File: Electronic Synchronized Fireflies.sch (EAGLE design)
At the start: 30 parts, among them J1 2WIRE_HEADER, J2 3WIRE_HEADER, Q1 BSS123, Q2 BSS84, Q3 LPT80A, Q4 LPT80A, Q5 LPT80A, U1 NCP1400A, U2 MSP430G2231

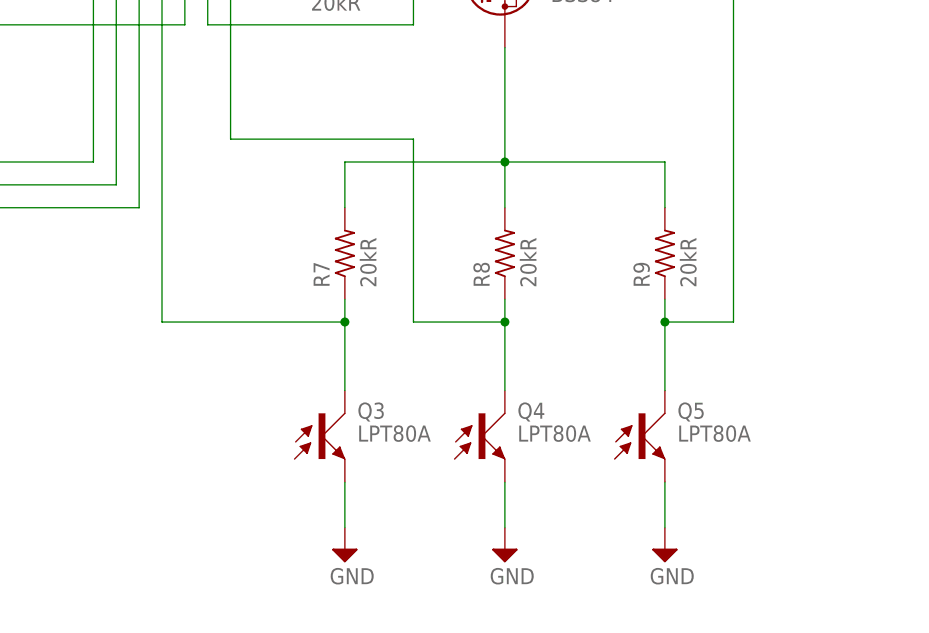
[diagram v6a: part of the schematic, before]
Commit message: Move back to LDR setup
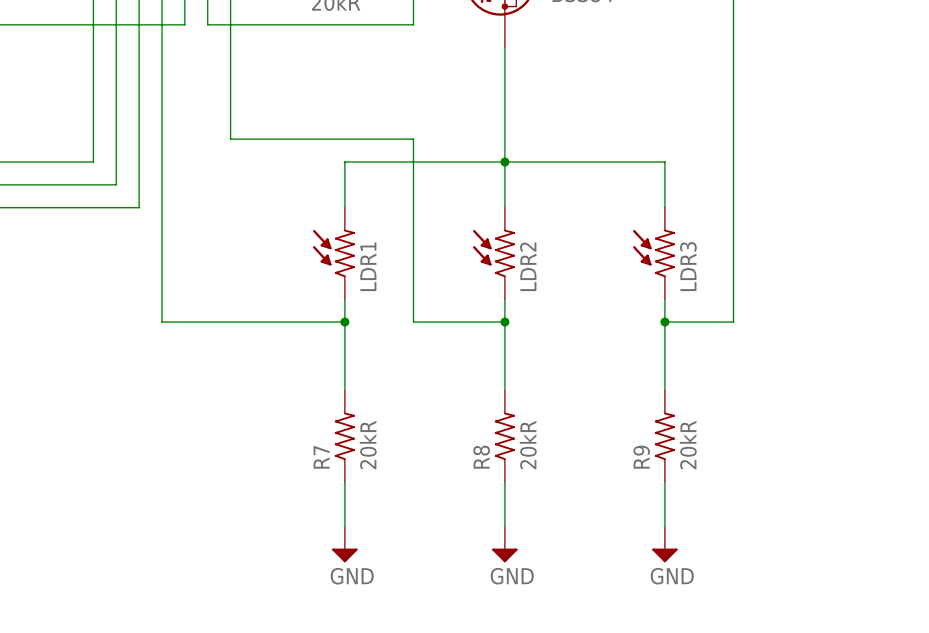
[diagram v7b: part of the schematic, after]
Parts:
- removed Q3, Q4, Q5: LPT80A, Electronic Synchronized Fireflies:LPT80ARTANGLEHOLDER
- added LDR1, LDR2, LDR3: LDRRTANGLEHOLDER, Electronic Synchronized Fireflies:LDRRTANGLEHOLDER
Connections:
- removed net N$14: Q3.C, R7.P$1, U2.6
- new net N$8: LDR1.1, R7.P$2, U2.6
- net GND: now also R7.P$1, R8.P$1, R9.P$1; no longer Q3.E, Q4.E, Q5.E
- net N$12: now also LDR1.2, LDR2.2, LDR3.2; no longer R7.P$2, R8.P$2, R9.P$2
- net N$13: now also LDR2.1, R8.P$2; no longer Q4.C, R8.P$1
- net N$15: now also LDR3.1, R9.P$2; no longer Q5.C, R9.P$1
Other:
- moved on the sheet: R7, R8, R9
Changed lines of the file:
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@@
 <part name="D5" library="Electronic Synchronized Fireflies" deviceset="LED" device="RTANGLEHOLDER" value="LED"/>
 <part name="D6" library="Electronic Synchronized Fireflies" deviceset="LED" device="RTANGLEHOLDER" value="LED"/>
-<part name="Q3" library="Electronic Synchronized Fireflies" deviceset="LPT80A" device="RTANGLEHOLDER" value="LPT80A"/>
-<part name="Q4" library="Electronic Synchronized Fireflies" deviceset="LPT80A" device="RTANGLEHOLDER" value="LPT80A"/>
-<part name="Q5" library="Electronic Synchronized Fireflies" deviceset="LPT80A" device="RTANGLEHOLDER" value="LPT80A"/>
+<part name="LDR1" library="Electronic Synchronized Fireflies" deviceset="LDR" device="RTANGLEHOLDER"/>
+<part name="LDR2" library="Electronic Synchronized Fireflies" deviceset="LDR" device="RTANGLEHOLDER"/>
+<part name="LDR3" library="Electronic Synchronized Fireflies" deviceset="LDR" device="RTANGLEHOLDER"/>
 </parts>
 <sheets>
@@
 <instance part="R5" gate="G$1" x="116.84" y="78.74" rot="R90"/>
 <instance part="R6" gate="G$1" x="129.54" y="78.74" rot="R90"/>
-<instance part="R7" gate="G$1" x="185.42" y="83.82" rot="R90"/>
-<instance part="R8" gate="G$1" x="203.2" y="83.82" rot="R90"/>
-<instance part="R9" gate="G$1" x="220.98" y="83.82" rot="R90"/>
+<instance part="R7" gate="G$1" x="185.42" y="63.5" rot="R90"/>
+<instance part="R8" gate="G$1" x="203.2" y="63.5" rot="R90"/>
+<instance part="R9" gate="G$1" x="220.98" y="63.5" rot="R90"/>
 <instance part="SUPPLY8" gate="GND" x="104.14" y="50.8"/>
 <instance part="SUPPLY9" gate="GND" x="116.84" y="50.8"/>
@@
 <instance part="D5" gate="G$1" x="116.84" y="60.96"/>
 <instance part="D6" gate="G$1" x="129.54" y="60.96"/>
-<instance part="Q3" gate="1" x="182.88" y="63.5"/>
-<instance part="Q4" gate="1" x="200.66" y="63.5"/>
-<instance part="Q5" gate="1" x="218.44" y="63.5"/>
+<instance part="LDR1" gate="G$1" x="185.42" y="83.82" rot="R90"/>
+<instance part="LDR2" gate="G$1" x="203.2" y="83.82" rot="R90"/>
+<instance part="LDR3" gate="G$1" x="220.98" y="83.82" rot="R90"/>
 </instances>
 <busses>
@@
 <pinref part="SUPPLY11" gate="GND" pin="GND"/>
 <wire x1="185.42" y1="58.42" x2="185.42" y2="53.34" width="0.1524" layer="91"/>
-<pinref part="Q3" gate="1" pin="E"/>
+<pinref part="R7" gate="G$1" pin="P$1"/>
 </segment>
 <segment>
 <pinref part="SUPPLY12" gate="GND" pin="GND"/>
 <wire x1="203.2" y1="58.42" x2="203.2" y2="53.34" width="0.1524" layer="91"/>
-<pinref part="Q4" gate="1" pin="E"/>
+<pinref part="R8" gate="G$1" pin="P$1"/>
 </segment>
 <segment>
 <pinref part="SUPPLY13" gate="GND" pin="GND"/>
 <wire x1="220.98" y1="53.34" x2="220.98" y2="58.42" width="0.1524" layer="91"/>
-<pinref part="Q5" gate="1" pin="E"/>
+<pinref part="R9" gate="G$1" pin="P$1"/>
 </segment>
 <segment>
@@
 <wire x1="203.2" y1="106.68" x2="203.2" y2="93.98" width="0.1524" layer="91"/>
 <wire x1="203.2" y1="93.98" x2="185.42" y2="93.98" width="0.1524" layer="91"/>
-<pinref part="R7" gate="G$1" pin="P$2"/>
-<wire x1="185.42" y1="93.98" x2="185.42" y2="88.9" width="0.1524" layer="91"/>
-<pinref part="R8" gate="G$1" pin="P$2"/>
+<junction x="203.2" y="93.98"/>
+<wire x1="220.98" y1="93.98" x2="203.2" y2="93.98" width="0.1524" layer="91"/>
+<wire x1="185.42" y1="88.9" x2="185.42" y2="93.98" width="0.1524" layer="91"/>
 <wire x1="203.2" y1="88.9" x2="203.2" y2="93.98" width="0.1524" layer="91"/>
-<junction x="203.2" y="93.98"/>
-<pinref part="R9" gate="G$1" pin="P$2"/>
 <wire x1="220.98" y1="88.9" x2="220.98" y2="93.98" width="0.1524" layer="91"/>
-<wire x1="220.98" y1="93.98" x2="203.2" y2="93.98" width="0.1524" layer="91"/>
+<pinref part="LDR1" gate="G$1" pin="2"/>
+<pinref part="LDR2" gate="G$1" pin="2"/>
+<pinref part="LDR3" gate="G$1" pin="2"/>
 </segment>
 </net>
 <net name="N$13" class="0">
 <segment>
-<pinref part="R8" gate="G$1" pin="P$1"/>
-<wire x1="203.2" y1="78.74" x2="203.2" y2="76.2" width="0.1524" layer="91"/>
-<wire x1="203.2" y1="76.2" x2="203.2" y2="68.58" width="0.1524" layer="91"/>
-<wire x1="203.2" y1="76.2" x2="193.04" y2="76.2" width="0.1524" layer="91"/>
 <wire x1="193.04" y1="76.2" x2="193.04" y2="96.52" width="0.1524" layer="91"/>
-<junction x="203.2" y="76.2"/>
 <wire x1="193.04" y1="96.52" x2="172.72" y2="96.52" width="0.1524" layer="91"/>
 <wire x1="172.72" y1="96.52" x2="172.72" y2="137.16" width="0.1524" layer="91"/>
 <pinref part="U2" gate="G$1" pin="7"/>
 <wire x1="172.72" y1="137.16" x2="185.42" y2="137.16" width="0.1524" layer="91"/>
-<pinref part="Q4" gate="1" pin="C"/>
-</segment>
-</net>
-<net name="N$14" class="0">
-<segment>
-<pinref part="R7" gate="G$1" pin="P$1"/>
-<wire x1="185.42" y1="78.74" x2="185.42" y2="76.2" width="0.1524" layer="91"/>
-<wire x1="185.42" y1="76.2" x2="185.42" y2="68.58" width="0.1524" layer="91"/>
-<wire x1="185.42" y1="76.2" x2="165.1" y2="76.2" width="0.1524" layer="91"/>
-<wire x1="165.1" y1="76.2" x2="165.1" y2="139.7" width="0.1524" layer="91"/>
-<junction x="185.42" y="76.2"/>
-<pinref part="U2" gate="G$1" pin="6"/>
-<wire x1="165.1" y1="139.7" x2="185.42" y2="139.7" width="0.1524" layer="91"/>
-<pinref part="Q3" gate="1" pin="C"/>
+<wire x1="203.2" y1="78.74" x2="203.2" y2="76.2" width="0.1524" layer="91"/>
+<wire x1="203.2" y1="76.2" x2="203.2" y2="68.58" width="0.1524" layer="91"/>
+<pinref part="R8" gate="G$1" pin="P$2"/>
+<wire x1="193.04" y1="76.2" x2="203.2" y2="76.2" width="0.1524" layer="91"/>
+<junction x="203.2" y="76.2"/>
+<pinref part="LDR2" gate="G$1" pin="1"/>
 </segment>
 </net>
 <net name="N$15" class="0">
 <segment>
-<pinref part="R9" gate="G$1" pin="P$1"/>
-<wire x1="220.98" y1="68.58" x2="220.98" y2="76.2" width="0.1524" layer="91"/>
-<wire x1="220.98" y1="76.2" x2="220.98" y2="78.74" width="0.1524" layer="91"/>
-<wire x1="228.6" y1="76.2" x2="220.98" y2="76.2" width="0.1524" layer="91"/>
-<junction x="220.98" y="76.2"/>
 <pinref part="U2" gate="G$1" pin="8"/>
 <wire x1="220.98" y1="137.16" x2="228.6" y2="137.16" width="0.1524" layer="91"/>
 <wire x1="228.6" y1="137.16" x2="228.6" y2="76.2" width="0.1524" layer="91"/>
-<pinref part="Q5" gate="1" pin="C"/>
+<wire x1="220.98" y1="78.74" x2="220.98" y2="76.2" width="0.1524" layer="91"/>
+<wire x1="220.98" y1="68.58" x2="220.98" y2="76.2" width="0.1524" layer="91"/>
+<pinref part="R9" gate="G$1" pin="P$2"/>
+<wire x1="228.6" y1="76.2" x2="220.98" y2="76.2" width="0.1524" layer="91"/>
+<junction x="220.98" y="76.2"/>
+<pinref part="LDR3" gate="G$1" pin="1"/>
 </segment>
 </net>
@@
 </segment>
 </net>
+<net name="N$8" class="0">
+<segment>
+<wire x1="165.1" y1="76.2" x2="165.1" y2="139.7" width="0.1524" layer="91"/>
+<pinref part="U2" gate="G$1" pin="6"/>
+<wire x1="165.1" y1="139.7" x2="185.42" y2="139.7" width="0.1524" layer="91"/>
+<wire x1="185.42" y1="78.74" x2="185.42" y2="76.2" width="0.1524" layer="91"/>
+<wire x1="185.42" y1="76.2" x2="185.42" y2="68.58" width="0.1524" layer="91"/>
+<pinref part="R7" gate="G$1" pin="P$2"/>
+<wire x1="165.1" y1="76.2" x2="185.42" y2="76.2" width="0.1524" layer="91"/>
+<junction x="185.42" y="76.2"/>
+<pinref part="LDR1" gate="G$1" pin="1"/>
+</segment>
+</net>
